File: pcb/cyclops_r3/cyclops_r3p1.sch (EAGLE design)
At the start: 53 parts, among them Q1 SUM11006, Q2 N-MOSFETTO-262, U1 MCP4921, U2 317-N, U3 ADR03, U4 OP1177, U5 LM324N

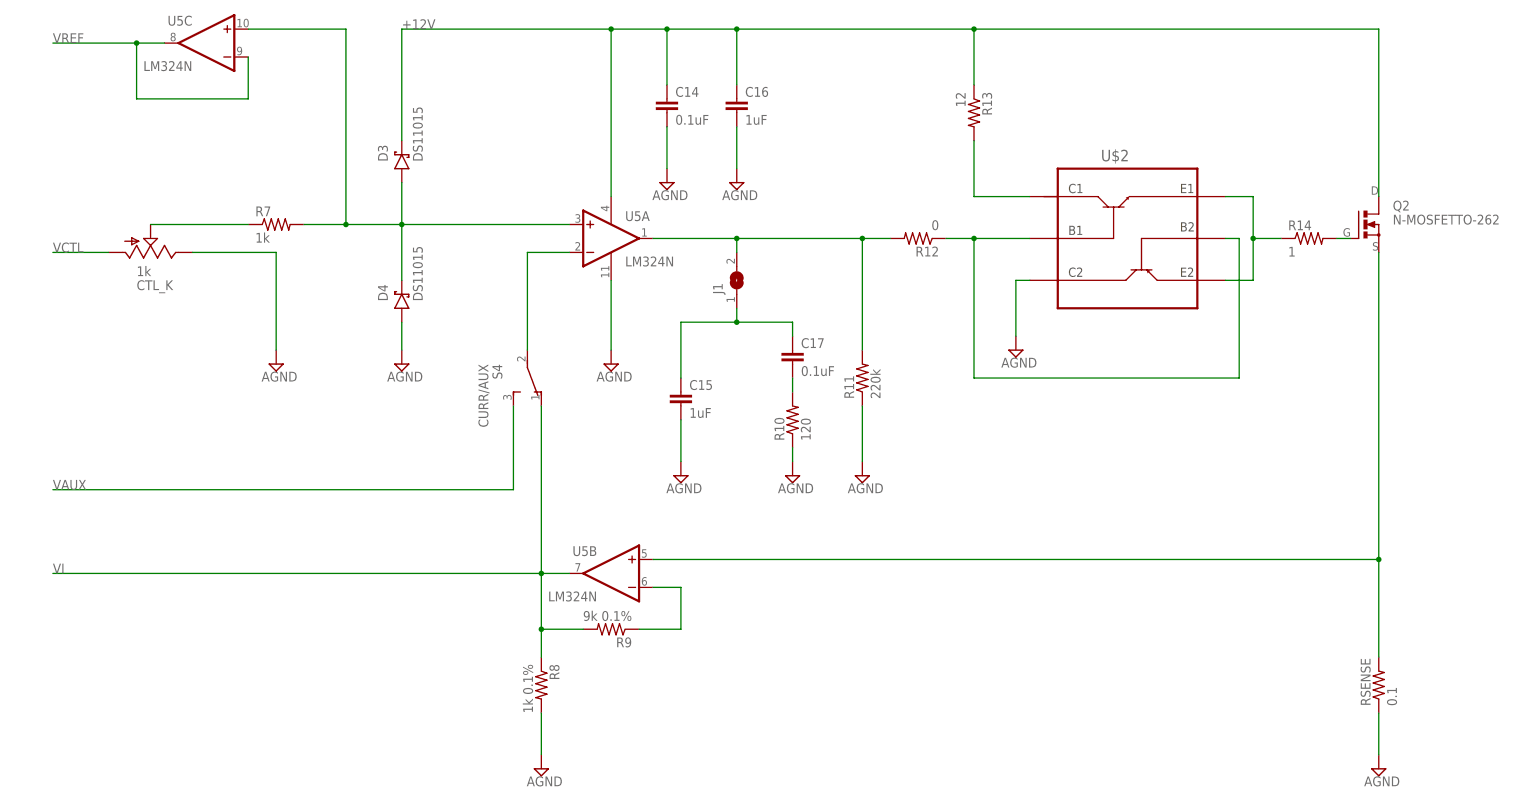
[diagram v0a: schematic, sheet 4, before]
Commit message: Silkscreen added to revision 3.1
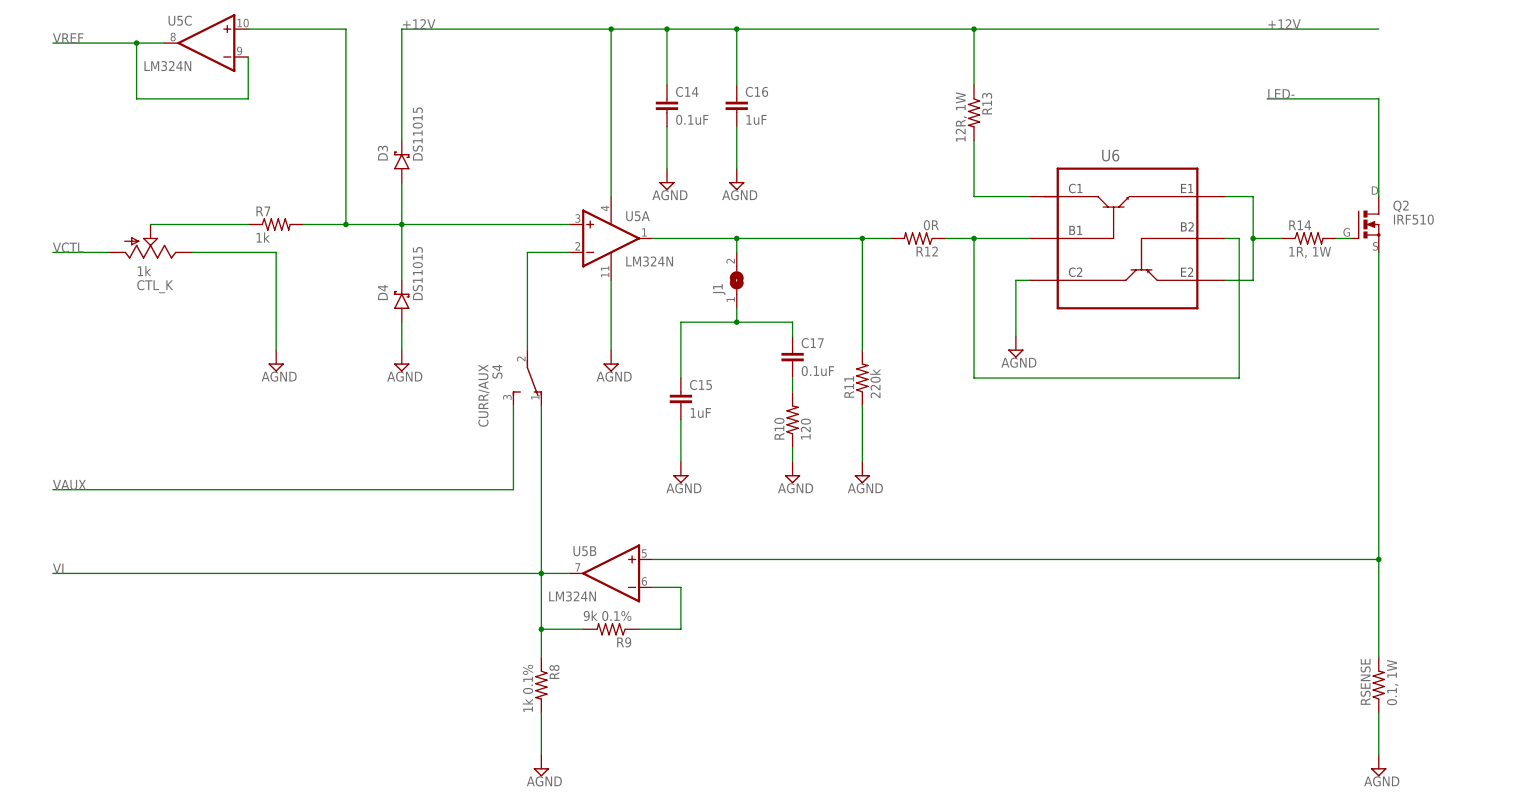
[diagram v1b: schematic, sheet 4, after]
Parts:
- Q2: value N-MOSFETTO-262 -> IRF510
- R12: value 0 -> 0R
- R13: value 12 -> 12R, 1W
- R14: value 1 -> 1R, 1W
- RSENSE: value 0.1 -> 0.1, 1W
- renumbered U$2 to U6
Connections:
- removed net AGND: U6.C2
- net +12V: no longer Q2.D
- net GND: now also U6.C2
- net LED-: now also Q2.D
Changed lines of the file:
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@@
 <attributes>
 <attribute name="DESIGNER" value="JONATHAN P. NEWMAN"/>
-<attribute name="DOC_NUMBER" value="1.0"/>
-<attribute name="REVISION" value="3.0"/>
+<attribute name="DOC_NUMBER" value="1.1"/>
+<attribute name="REVISION" value="3.1"/>
 </attributes>
 <variantdefs>
@@
 <part name="R9" library="cyclops" deviceset="R" device="_0603" value="9k 0.1%"/>
 <part name="R8" library="cyclops" deviceset="R" device="_0603" value="1k 0.1%"/>
-<part name="RSENSE" library="cyclops" deviceset="R" device="_2512" value="0.1"/>
+<part name="RSENSE" library="cyclops" deviceset="R" device="_2512" value="0.1, 1W"/>
 <part name="U3" library="cyclops" deviceset="ADR03AKSZ-REEL7" device="" value="ADR03"/>
 <part name="C10" library="cyclops" deviceset="C" device="_0805" value="1uF"/>
@@
 <part name="SUPPLY34" library="cyclops" deviceset="GND" device=""/>
 <part name="S3" library="cyclops" deviceset="SPDT" device="_CFPA" value="TEST"/>
-<part name="R12" library="cyclops" deviceset="R" device="_0603" value="0"/>
-<part name="U$2" library="cyclops" deviceset="ZXTD4591E6" device=""/>
+<part name="R12" library="cyclops" deviceset="R" device="_0603" value="0R"/>
+<part name="U6" library="cyclops" deviceset="ZXTD4591E6" device=""/>
 <part name="SUPPLY35" library="cyclops" deviceset="AGND" device=""/>
-<part name="R13" library="cyclops" deviceset="R" device="_0603" value="12"/>
-<part name="Q2" library="cyclops" deviceset="N-MOSFET" device="TO-262"/>
-<part name="R14" library="cyclops" deviceset="R" device="_0603" value="1"/>
+<part name="R13" library="cyclops" deviceset="R" device="_0603" value="12R, 1W"/>
+<part name="Q2" library="cyclops" deviceset="N-MOSFET" device="TO-262" value="IRF510"/>
+<part name="R14" library="cyclops" deviceset="R" device="_0603" value="1R, 1W"/>
 </parts>
 <sheets>
@@
 <instance part="SUPPLY1" gate="G$1" x="81.28" y="40.64"/>
 <instance part="R12" gate="R" x="91.44" y="83.82" rot="R180"/>
-<instance part="U$2" gate="G$1" x="129.54" y="83.82"/>
+<instance part="U6" gate="G$1" x="129.54" y="83.82"/>
 <instance part="SUPPLY35" gate="G$1" x="109.22" y="63.5"/>
 <instance part="R13" gate="R" x="101.6" y="106.68" rot="R270"/>
@@
 <pinref part="SUPPLY1" gate="G$1" pin="AGND"/>
 <wire x1="81.28" y1="53.34" x2="81.28" y2="43.18" width="0.1524" layer="91"/>
+</segment>
+<segment>
+<pinref part="SUPPLY35" gate="G$1" pin="AGND"/>
+<wire x1="109.22" y1="66.04" x2="109.22" y2="76.2" width="0.1524" layer="91"/>
+<pinref part="U6" gate="G$1" pin="C2"/>
+<wire x1="109.22" y1="76.2" x2="111.76" y2="76.2" width="0.1524" layer="91"/>
 </segment>
 </net>
@@
 <pinref part="R13" gate="R" pin="1"/>
 <wire x1="101.6" y1="111.76" x2="101.6" y2="121.92" width="0.1524" layer="91"/>
-<pinref part="Q2" gate="G$1" pin="D"/>
 <wire x1="101.6" y1="121.92" x2="175.26" y2="121.92" width="0.1524" layer="91"/>
-<wire x1="175.26" y1="121.92" x2="175.26" y2="91.44" width="0.1524" layer="91"/>
 <junction x="101.6" y="121.92"/>
+<label x="154.94" y="121.92" size="1.778" layer="95"/>
 </segment>
 </net>
@@
 <segment>
 <pinref part="R12" gate="R" pin="1"/>
-<pinref part="U$2" gate="G$1" pin="B1"/>
+<pinref part="U6" gate="G$1" pin="B1"/>
 <wire x1="96.52" y1="83.82" x2="101.6" y2="83.82" width="0.1524" layer="91"/>
 <wire x1="101.6" y1="83.82" x2="111.76" y2="83.82" width="0.1524" layer="91"/>
@@
 <wire x1="101.6" y1="58.42" x2="149.86" y2="58.42" width="0.1524" layer="91"/>
 <wire x1="149.86" y1="58.42" x2="149.86" y2="83.82" width="0.1524" layer="91"/>
-<pinref part="U$2" gate="G$1" pin="B2"/>
+<pinref part="U6" gate="G$1" pin="B2"/>
 <wire x1="149.86" y1="83.82" x2="147.32" y2="83.82" width="0.1524" layer="91"/>
 </segment>
 </net>
-<net name="AGND" class="0">
-<segment>
-<pinref part="SUPPLY35" gate="G$1" pin="AGND"/>
-<wire x1="109.22" y1="66.04" x2="109.22" y2="76.2" width="0.1524" layer="91"/>
-<pinref part="U$2" gate="G$1" pin="C2"/>
-<wire x1="109.22" y1="76.2" x2="111.76" y2="76.2" width="0.1524" layer="91"/>
-</segment>
-</net>
 <net name="N$10" class="0">
 <segment>
-<pinref part="U$2" gate="G$1" pin="E1"/>
+<pinref part="U6" gate="G$1" pin="E1"/>
 <wire x1="147.32" y1="91.44" x2="152.4" y2="91.44" width="0.1524" layer="91"/>
-<pinref part="U$2" gate="G$1" pin="E2"/>
+<pinref part="U6" gate="G$1" pin="E2"/>
 <wire x1="152.4" y1="91.44" x2="152.4" y2="83.82" width="0.1524" layer="91"/>
 <wire x1="152.4" y1="83.82" x2="152.4" y2="76.2" width="0.1524" layer="91"/>
@@
 <net name="N$12" class="1">
 <segment>
-<pinref part="U$2" gate="G$1" pin="C1"/>
+<pinref part="U6" gate="G$1" pin="C1"/>
 <wire x1="101.6" y1="91.44" x2="111.76" y2="91.44" width="0.1524" layer="91"/>
 <pinref part="R13" gate="R" pin="2"/>
@@
 </segment>
 </net>
+<net name="LED-" class="0">
+<segment>
+<pinref part="Q2" gate="G$1" pin="D"/>
+<wire x1="175.26" y1="91.44" x2="175.26" y2="109.22" width="0.1524" layer="91"/>
+<wire x1="175.26" y1="109.22" x2="154.94" y2="109.22" width="0.1524" layer="91"/>
+<label x="154.94" y="109.22" size="1.778" layer="95"/>
+</segment>
+</net>

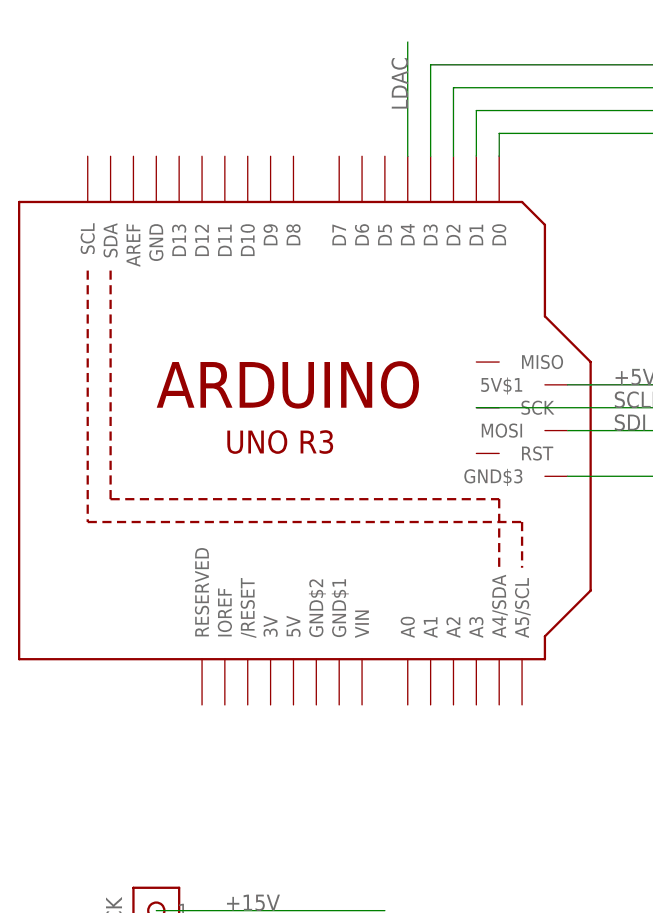
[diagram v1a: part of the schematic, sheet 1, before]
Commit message: Some updates to the library and board. Also, update the design rules so that vias are not exposed solder.
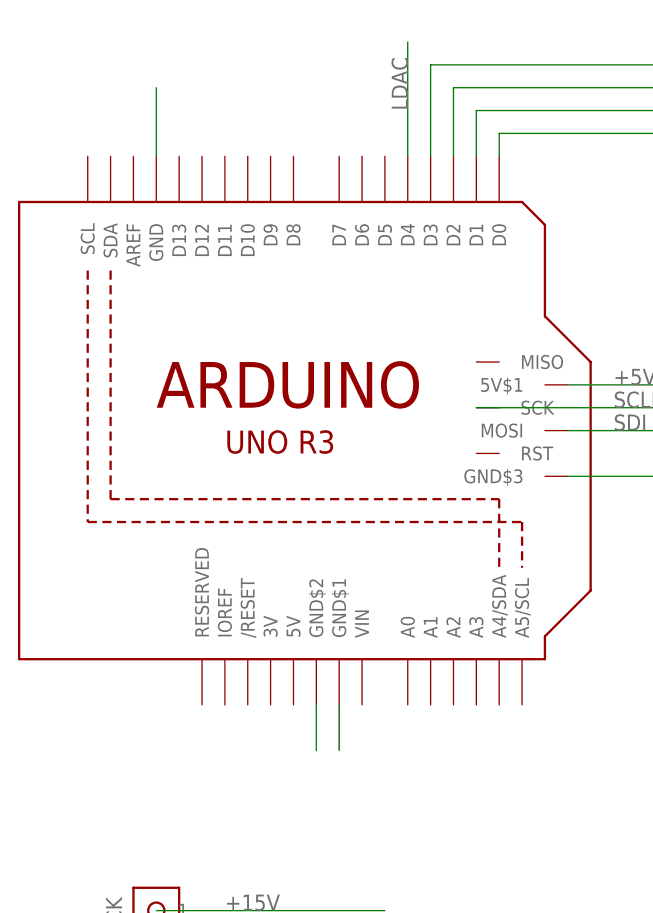
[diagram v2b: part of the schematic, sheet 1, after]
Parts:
- D2: device cyclops:DIODE-RECTS1B-13-F -> cyclops:DIODES1B-13-F
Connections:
- net GND: now also U$1.GND, U$1.GND$1, U$1.GND$2
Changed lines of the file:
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@@
 <part name="U$1" library="cyclops" deviceset="ARDUINO_R3_ICSP" device=""/>
 <part name="U2" library="cyclops" deviceset="*317" device="_TO263" value="317-N"/>
-<part name="D2" library="cyclops" deviceset="DIODE-RECT" device="S1B-13-F" value="S1B-13-F"/>
+<part name="D2" library="cyclops" deviceset="DIODE" device="S1B-13-F" value="S1B-13-F"/>
 <part name="R3" library="cyclops" deviceset="R" device="_0603" value="1.8k"/>
 <part name="R4" library="cyclops" deviceset="R" device="_0603" value="240k"/>
@@
 <pinref part="SUPPLY12" gate="G$1" pin="AGND"/>
 </segment>
-</net>
+<segment>
+<pinref part="U$1" gate="G$1" pin="GND$2"/>
+<wire x1="60.96" y1="17.78" x2="60.96" y2="12.7" width="0.1524" layer="91"/>
+</segment>
+<segment>
+<pinref part="U$1" gate="G$1" pin="GND$1"/>
+<wire x1="63.5" y1="17.78" x2="63.5" y2="12.7" width="0.1524" layer="91"/>
+</segment>
+<segment>
+<pinref part="U$1" gate="G$1" pin="GND"/>
+<wire x1="43.18" y1="78.74" x2="43.18" y2="86.36" width="0.1524" layer="91"/>
+</segment>
+</net>

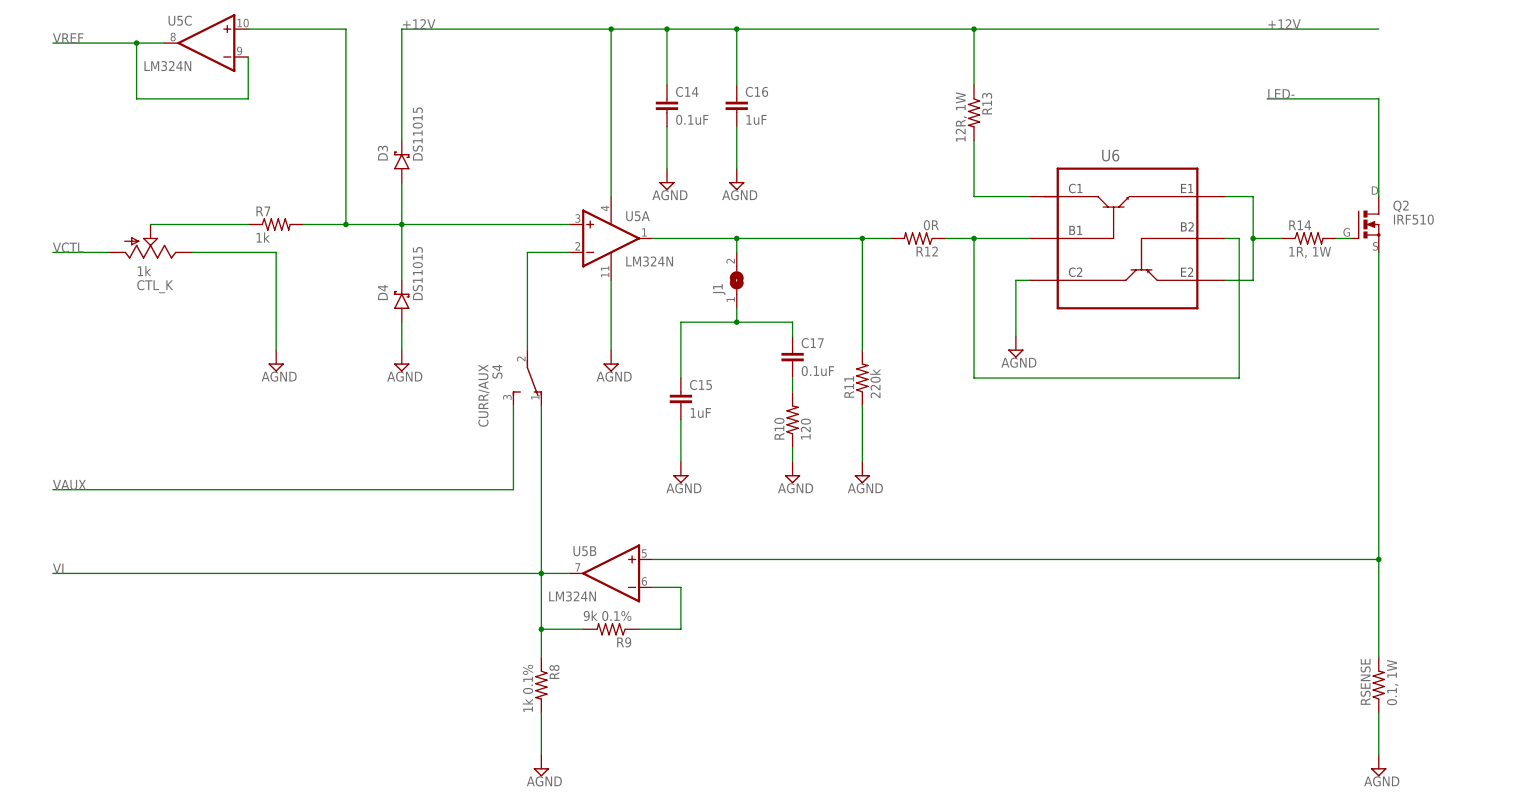
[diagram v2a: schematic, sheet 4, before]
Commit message: Reimplemented NMOS bias network after merge issues.
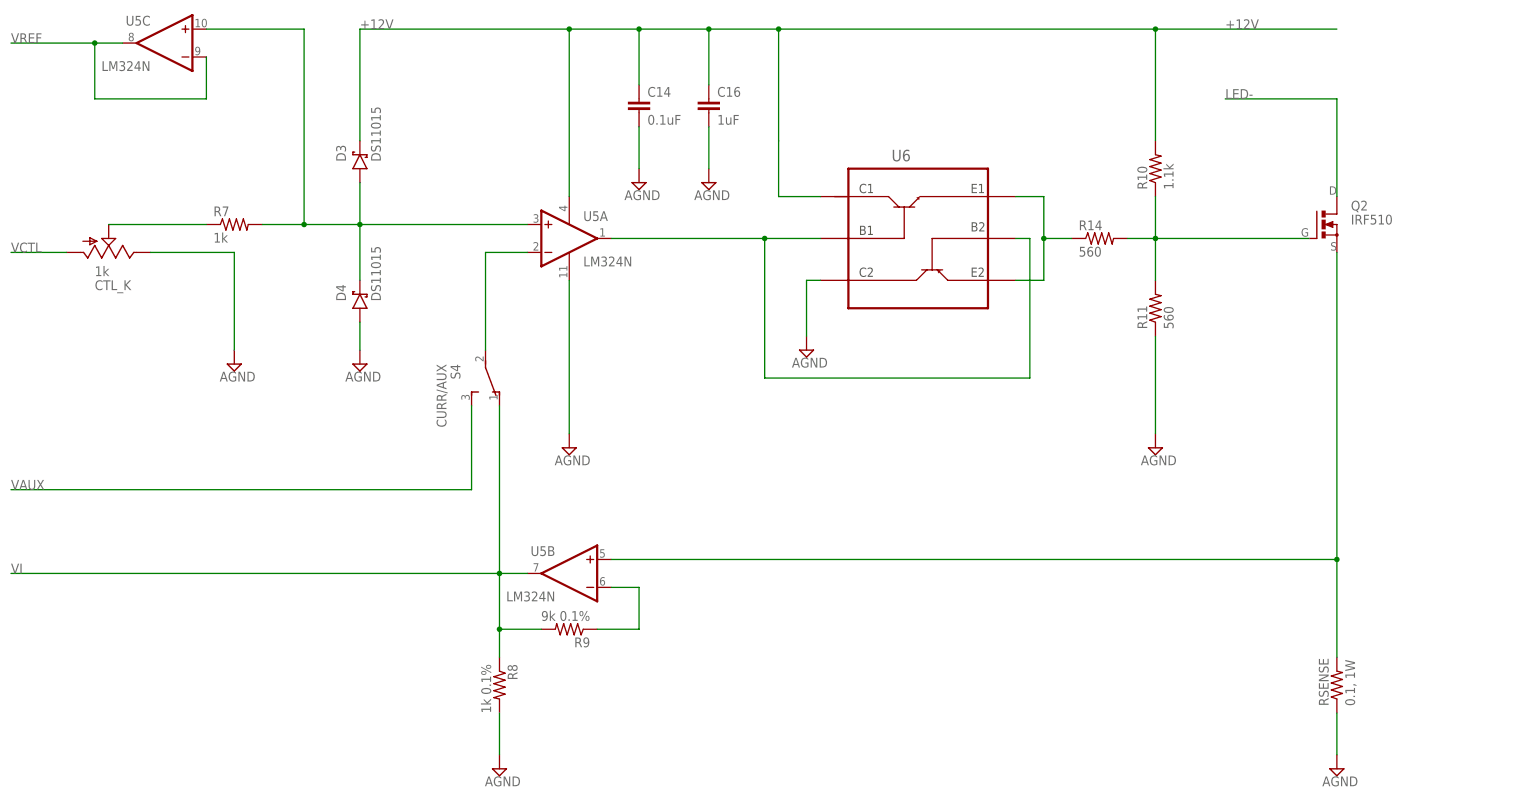
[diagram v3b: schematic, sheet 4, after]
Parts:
- removed C15: 1uF, cyclops:C_0805
- removed C17: 0.1uF, cyclops:C_0603
- removed J1: (no value), jumper:SJ
- removed R12: 0R, cyclops:R_0603
- removed R13: 12R, 1W, cyclops:R_0603
- R10: value 120 -> 1.1k
- R11: value 220k -> 560
- R14: value 1R, 1W -> 560
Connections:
- removed net N$11: C15.1, C17.1, J1.1
- removed net N$4: C17.2, R10.2
- removed net N$9: R12.1, U6.B1, U6.B2
- new net AGND: R11.1
- net +12V: now also R10.2; no longer R13.1
- net GND: no longer C15.2, R10.1, R11.1
- net N$12: no longer R13.2
- net N$13: now also R10.1, R11.2
- net N$3: now also U6.B1, U6.B2; no longer J1.2, R11.2, R12.2
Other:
- moved on the sheet: C14, C16, CTL_K, D3, D4, Q2, R10, R11, R14, R7, R8, R9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
